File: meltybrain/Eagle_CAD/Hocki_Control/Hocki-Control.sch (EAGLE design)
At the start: 1 part, among them U1 TEENSY_4.1

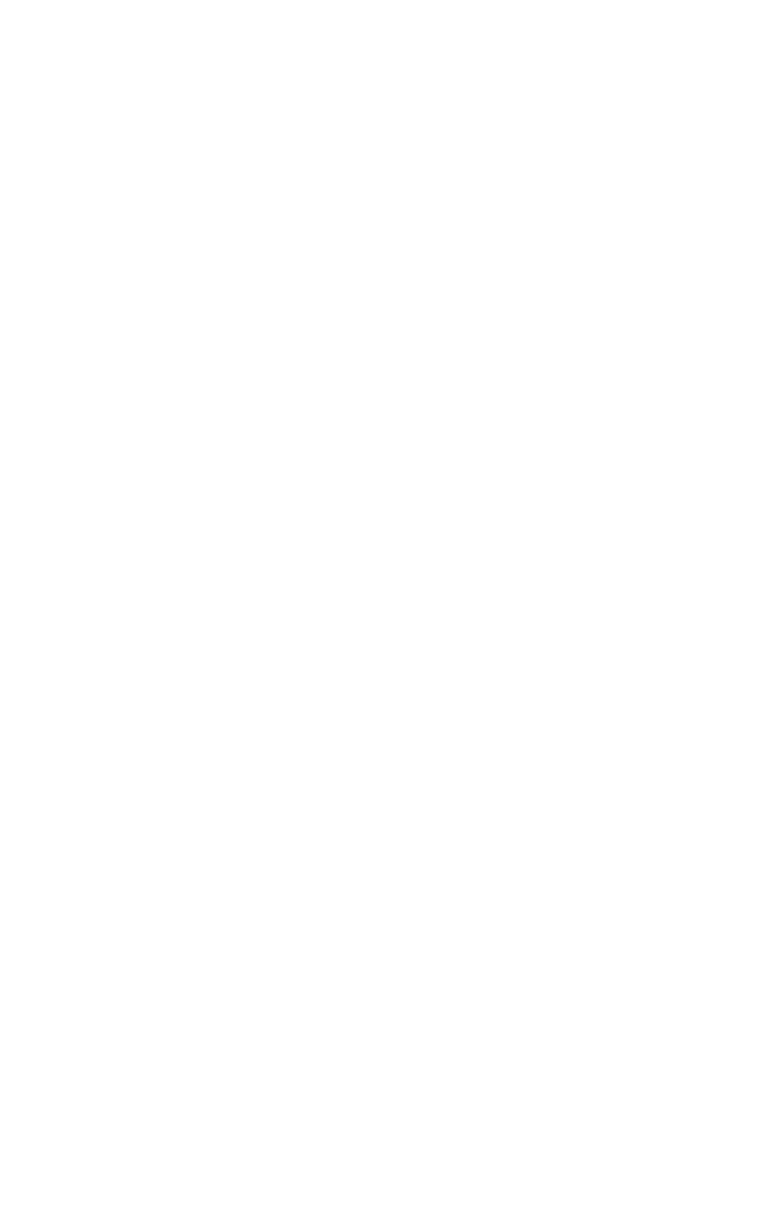
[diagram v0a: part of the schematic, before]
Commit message: added accelerometers to schematic
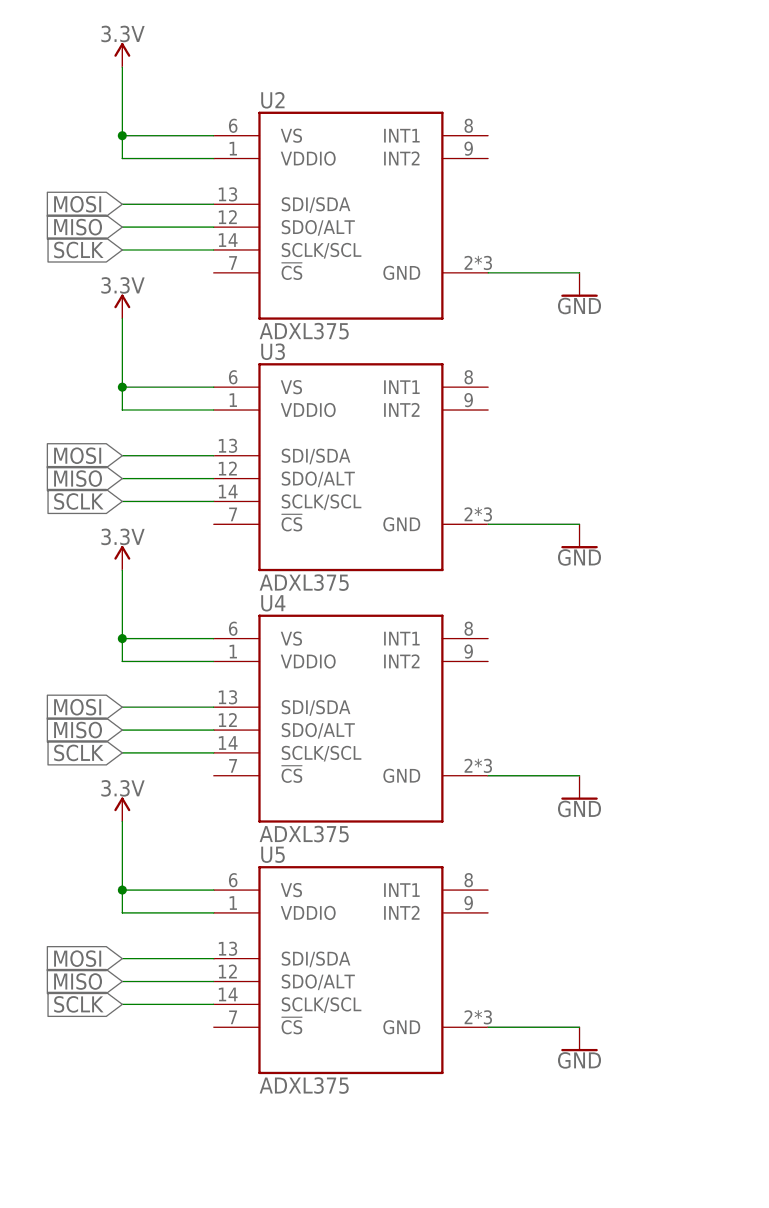
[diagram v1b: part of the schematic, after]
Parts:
- added U2, U3, U4, U5: ADXL375, Hocki_library:ADXL375
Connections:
- new net 3.3V: U2.VDDIO, U2.VS, U3.VDDIO, U3.VS, U4.VDDIO, U4.VS, U5.VDDIO, U5.VS
- new net GND: U2.GND, U3.GND, U4.GND, U5.GND
- new net MISO: U2.SDO/ALT, U3.SDO/ALT, U4.SDO/ALT, U5.SDO/ALT
- new net MOSI: U2.SDI/SDA, U3.SDI/SDA, U4.SDI/SDA, U5.SDI/SDA
- new net SCLK: U2.SCLK/SCL, U3.SCLK/SCL, U4.SCLK/SCL, U5.SCLK/SCL

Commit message: added bandpass filter to control and updated ir
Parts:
- added C1, C2: 100n, rcl:C-USC0603
- added C3, C4: 50n, rcl:C-USC0603
- added C5, C6: 60n, rcl:C-USC0603
- added D1, D2: RB521S30T1G, Hocki_library:RB521S30T1G
- added R1, R15, R18, R19: 50, rcl:R-US_R0603
- added R10, R11, R4, R5: 4.5k, rcl:R-US_R0603
- added R12, R13, R14, R3, R6, R7, R8, R9: 160, rcl:R-US_R0603
- added R16, R17: 45.25k, rcl:R-US_R0603
- added R2: 500, rcl:R-US_R0603
- added U10: TLV3502AIDCNR, Hocki_library:TLV3502AIDCNR
- added U6, U7, U8, U9: LMH6612MAX/NOPB, Hocki_library:LMH6612MAX/NOPB
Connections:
- new net 10K_INT: U10.OUTA, U10.OUTB
- new net 10K_PEAK: C6.1, D1.C, R17.2, U10.INA+, U9.INA-
- new net 10K_REF: U10.INA-
- new net 2.5V_REF: C2.2, C4.2, R10.1, R13.1, R4.1, R7.1, U6.INB-, U6.OUTB
- new net 20K_PEAK: C5.1, D2.C, R16.2, U10.INB+, U9.INB-
- new net 20K_REF: U10.INB-
- new net 5V: U6.V+, U7.V+, U8.V+, U9.V+
- new net N$1: R11.2, R5.2, U6.INA-, U6.OUTA
- new net N$10: C3.1, R12.1, U8.INA-, U8.INB-
- new net N$11: C4.1, R10.2, R11.1, R9.1, U8.INA+
- new net N$12: R12.2, R14.1, U8.OUTA, U9.INB+
- new net N$13: R13.2, R14.2, U8.INB+
- new net N$14: D1.A, R1.2, R18.1
- new net N$15: D2.A, R15.2, R19.1
- new net N$2: R1.1, U9.OUTA
- new net N$3: C1.2, R3.2, U7.OUTB
- new net N$4: C1.1, R6.1, U7.INA-, U7.INB-
- new net N$5: C2.1, R3.1, R4.2, R5.1, U7.INA+
- new net N$6: R6.2, R8.1, U7.OUTA, U9.INA+
- new net N$7: R7.2, R8.2, U7.INB+
- new net N$8: C3.2, R9.2, U8.OUTB
- new net N$9: R15.1, U9.OUTB
- new net VG_SIGNAL1: R2.2, U6.INA+
- net 3.3V: now also U10.V+
- net GND: now also C5.2, C6.2, R16.1, R17.1, R18.2, R19.2, R2.1, U10.V-, U6.V-, U7.V-, U8.V-, U9.V-
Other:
- moved on the sheet: U1, U2, U3, U4, U5

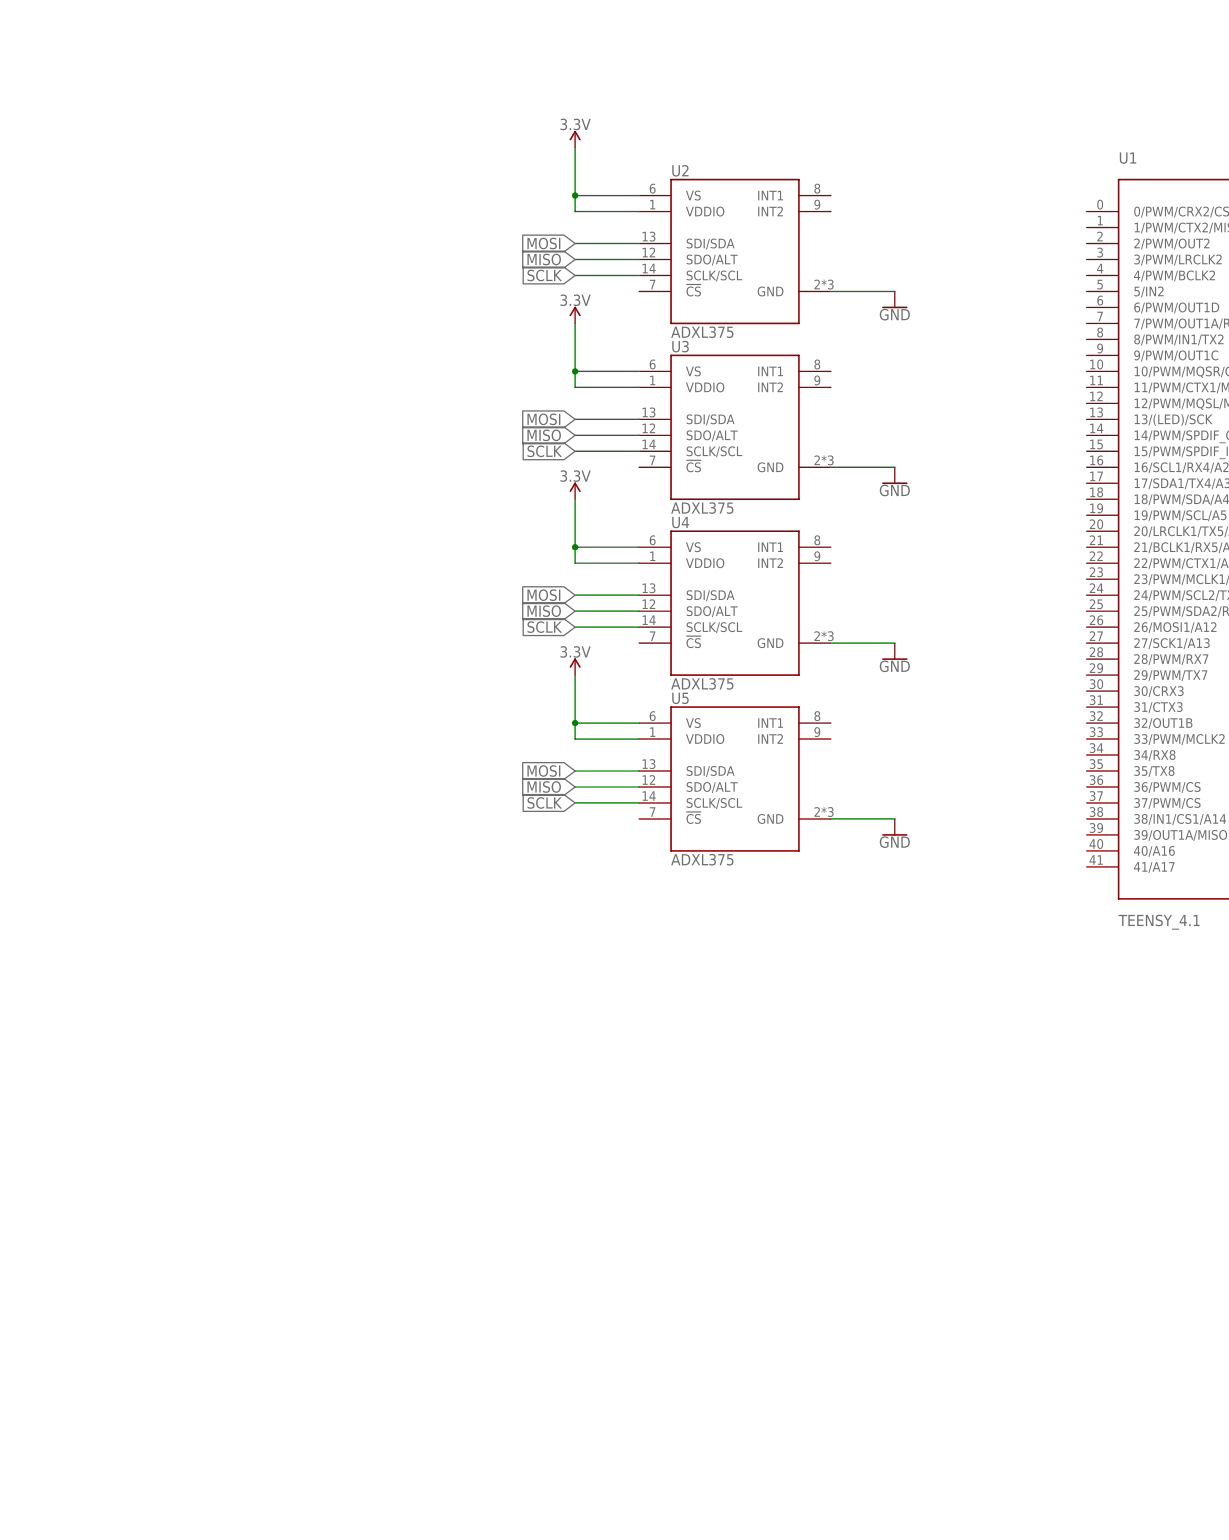
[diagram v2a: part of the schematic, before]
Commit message: magnetometer and accelerometer to schematic
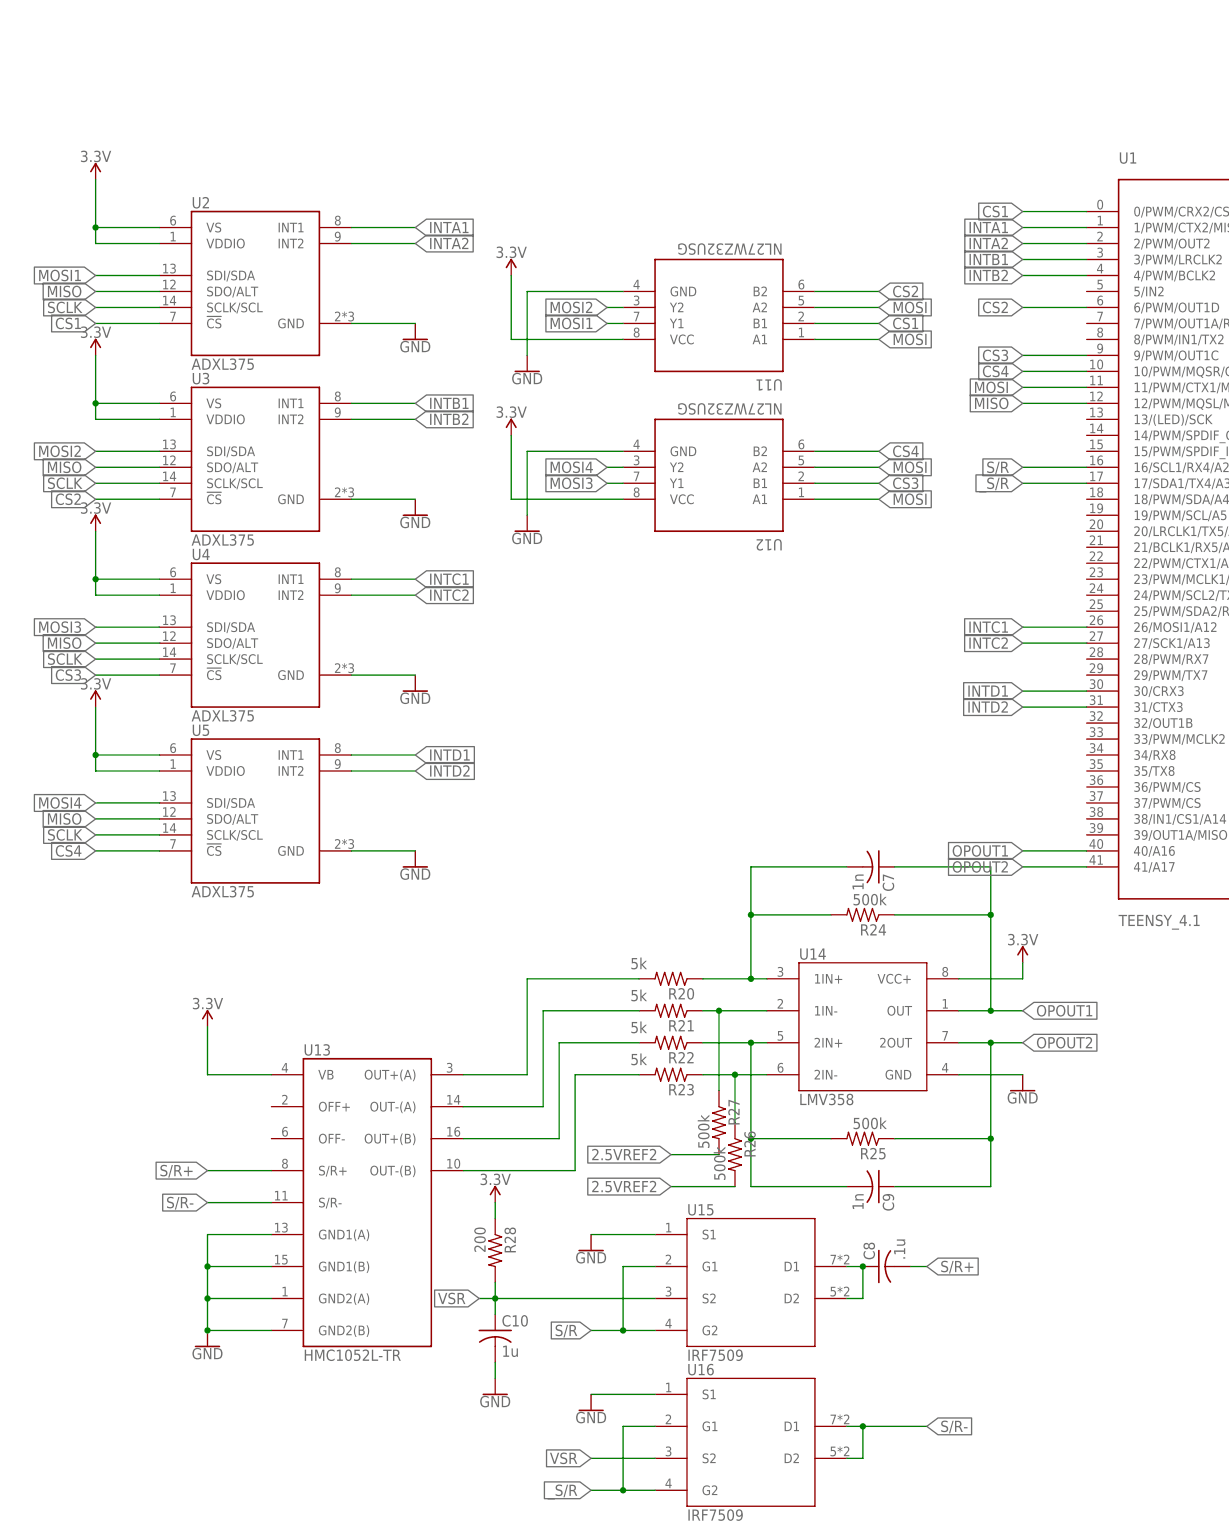
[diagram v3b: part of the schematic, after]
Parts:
- added C10: 1u, rcl:C-USC0603
- added C7, C9: 1n, rcl:C-USC0603
- added C8: .1u, rcl:C-USC0603
- added R20, R21, R22, R23: 5k, rcl:R-US_R0603
- added R24, R25, R26, R27: 500k, rcl:R-US_R0603
- added R28: 200, rcl:R-US_R0603
- added U11, U12: NL27WZ32USG, Hocki_library:NL27WZ32USG
- added U13: HMC1052L-TR, Hocki_library:HMC1052L-TR
- added U14: LMV358, Hocki_library:LMV358
- added U15, U16: IRF7509, Hocki_library:IRF7509
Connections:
- new net 2.5VREF2: R26.2, R27.2
- new net CS1: U1.0/PWM/CRX2/CS1/RX1, U11.B1, U2.!CS
- new net CS2: U1.6/PWM/OUT1D, U11.B2, U3.!CS
- new net CS3: U1.9/PWM/OUT1C, U12.B1, U4.!CS
- new net CS4: U1.10/PWM/MQSR/CS, U12.B2, U5.!CS
- new net INTA1: U1.1/PWM/CTX2/MISO1/TX1, U2.INT1
- new net INTA2: U1.2/PWM/OUT2, U2.INT2
- new net INTB1: U1.3/PWM/LRCLK2, U3.INT1
- new net INTB2: U1.4/PWM/BCLK2, U3.INT2
- new net INTC1: U1.26/MOSI1/A12, U4.INT1
- new net INTC2: U1.27/SCK1/A13, U4.INT2
- new net INTD1: U1.30/CRX3, U5.INT1
- new net INTD2: U1.31/CTX3, U5.INT2
- new net MOSI1: U11.Y1, U2.SDI/SDA
- new net MOSI2: U11.Y2, U3.SDI/SDA
- new net MOSI3: U12.Y1, U4.SDI/SDA
- new net MOSI4: U12.Y2, U5.SDI/SDA
- new net N$16: C8.1, U15.D1, U15.D2
- new net N$17: R21.2, U13.OUT-(A)
- new net N$18: R22.2, U13.OUT+(B)
- new net N$19: R23.2, U13.OUT-(B)
- new net N$34: R23.1, R26.1, U14.2IN-
- new net N$35: C9.2, R22.1, R25.2, U14.2IN+
- new net N$36: R21.1, R27.1, U14.1IN-
- new net N$37: C7.2, R20.1, R24.2, U14.1IN+
- new net OPOUT1: C7.1, R24.1, U1.40/A16, U14.OUT
- new net OPOUT2: C9.1, R25.1, U1.41/A17, U14.2OUT
- new net OUT+(A): R20.2, U13.OUT+(A)
- new net S/R: U1.16/SCL1/RX4/A2, U15.G1, U15.G2
- new net S/R+: C8.2, U13.S/R+
- new net S/R-: U13.S/R-, U16.D1, U16.D2
- new net VSR: C10.1, R28.2, U15.S2, U16.S2
- new net _S/R: U1.17/SDA1/TX4/A3, U16.G1, U16.G2
- net 3.3V: now also R28.1, U11.VCC, U12.VCC, U13.VB, U14.VCC+
- net GND: now also C10.2, U11.GND, U12.GND, U13.GND1(A), U13.GND1(B), U13.GND2(A), U13.GND2(B), U14.GND, U15.S1, U16.S1
- net MISO: now also U1.12/PWM/MQSL/MISO
- net MOSI: now also U1.11/PWM/CTX1/MOSI, U11.A1, U11.A2, U12.A1, U12.A2; no longer U2.SDI/SDA, U3.SDI/SDA, U4.SDI/SDA, U5.SDI/SDA
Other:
- moved on the sheet: U2, U3, U4, U5

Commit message: finished sensor circuits on control
IR mux
cleaned acc
magnetometer vref; did not need second set of mosfets
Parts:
- added C11, C12: 1u, rcl:C-USC0603
- added R29, R30, R33, R34, R35: 500, rcl:R-US_R0603
- added R31, R32: 5k, rcl:R-US_R0603
- added U17: LMH6612MAX/NOPB, Hocki_Library:LMH6612MAX/NOPB
- D1, D2: device Hocki_library:RB521S30T1G -> Hocki_Library:RB521S30T1G
- U1: device Hocki_library:TEENSY_4.1 -> Hocki_Library:TEENSY_4.1
- U10: device Hocki_library:TLV3502AIDCNR -> Hocki_Library:TLV3502AIDCNR
- U11, U12: device Hocki_library:NL27WZ32USG -> Hocki_Library:NL27WZ32USG
- U13: device Hocki_library:HMC1052L-TR -> Hocki_Library:HMC1052L-TR
- U14: device Hocki_library:LMV358 -> Hocki_Library:LMV358
- U15: device Hocki_library:IRF7509 -> Hocki_Library:IRF7509
- U16: value IRF7509 -> TMUX1219DCKR; device Hocki_library:IRF7509 -> Hocki_Library:TMUX1219DCKR
- U2, U3, U4, U5: device Hocki_library:ADXL375 -> Hocki_Library:ADXL375
- U6, U7, U8, U9: device Hocki_library:LMH6612MAX/NOPB -> Hocki_Library:LMH6612MAX/NOPB
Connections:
- net OPOUT1 renamed MAG_OUTPUTA
- net OPOUT2 renamed MAG_OUTPUTB
- removed net 2.5VREF2: R26.2, R27.2
- removed net S/R-: U13.S/R-, U16.D1, U16.D2
- new net 20K_INT: U1.23/PWM/MCLK1/CRX1/A9, U10.OUTB
- new net IR_BOTTOM: U16.S2
- new net IR_SEL: U1.17/SDA1/TX4/A3, U16.SEL
- new net IR_TOP: U16.S1
- new net N$20: R29.1, R30.2, U6.INB+
- new net N$21: R31.1, U1.18/PWM/SDA/A4
- new net N$22: R32.1, U1.19/PWM/SCL/A5
- new net N$23: R34.2, R35.1, U17.INA+, U17.INB+
- new net N$24: R33.1, U17.OUTB
- new net VREF/2: R26.2, R27.2, U17.INA-, U17.OUTA
- net 10K_INT: now also U1.22/PWM/CTX1/A8; no longer U10.OUTB
- net 10K_PEAK: now also U1.20/LRCLK1/TX5/A6
- net 10K_REF: now also C12.1, R31.2
- net 20K_PEAK: now also U1.21/BCLK1/RX5/A7
- net 20K_REF: now also C11.1, R32.2
- net 3.3V: now also R34.1, U17.V+
- net 5V: now also R29.2, U1.VIN, U16.V+
- net GND: now also C11.2, C12.2, R30.1, R33.2, R35.2, U1.GND, U13.OFF-, U13.S/R-, U16.GND, U17.INB-, U17.V-; no longer U16.S1
- net VG_SIGNAL1: now also U16.D
- net VSR: no longer U16.S2
- net _S/R: now also U1.15/PWM/SPDIF_IN/RX3/A1; no longer U1.17/SDA1/TX4/A3, U16.G1, U16.G2
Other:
- moved on the sheet: C1, C10, C2, C3, C4, C5, C6, C7, C8, C9, D1, D2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

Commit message: progress...
IR receiver has all parts accounting BoM
started doing that for control
progress on control layout
Varun I hate this...
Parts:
- removed R1, R15, R18, R19: 50, rcl:R-US_R0603
- added C13, C15: 0.5u, rcl:C-USC0603
- added C14, C16: 2u, rcl:C-USC0603
- added R36, R38: 5k, rcl:R-US_R0603
- added R37, R39: 820, rcl:R-US_R0603
- added U18: LMV358, Hocki_Library:LMV358
- C1, C2: value 100n -> 47n; device rcl:C-USC0603 -> rcl:C-USC1206
- C3, C4: value 50n -> 47n; device rcl:C-USC0603 -> rcl:C-USC1206
- R12, R13, R14, R9: value 160 -> 169
- R16, R17: value 45.25k -> 44.2k
- R2, R33, R34, R35: value 500 -> 499
- R29: value 500 -> 665
- R30: value 500 -> 330
- U17: value LMH6612MAX/NOPB -> LMV358; device Hocki_Library:LMH6612MAX/NOPB -> Hocki_Library:LMV358
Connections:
- net N$1 renamed VG_SIGNAL_BUF
- net N$12 renamed 20K_OUT
- net N$20 renamed 1.6V_REF
- net N$6 renamed 10K_OUT
- net VG_SIGNAL1 renamed VG_SIGNAL
- removed net 2.5V_REF: C2.2, C4.2, R10.1, R13.1, R4.1, R7.1, U6.INB-, U6.OUTB
- removed net N$11: C4.1, R10.2, R11.1, R9.1, U8.INA+
- removed net N$14: D1.A, R1.2, R18.1
- removed net N$15: D2.A, R15.2, R19.1
- removed net N$3: C1.2, R3.2, U7.OUTB
- removed net N$5: C2.1, R3.1, R4.2, R5.1, U7.INA+
- removed net N$8: C3.2, R9.2, U8.OUTB
- new net 1.66V_REF_BUF: C1.2, C3.2, R10.1, R13.1, R4.1, R7.1, U6.INB-, U6.OUTB
- new net 10K_FB: C2.2, R3.2, U7.OUTB
- new net 10K_IN: C1.1, R3.1, R4.2, R5.1, U7.INA+
- new net 20K_FB: C4.2, R9.2, U8.OUTB
- new net 20K_IN: C3.1, R10.2, R11.1, R9.1, U8.INA+
- new net MAG_FILT_A: C14.2, U1.40/A16, U18.1IN-, U18.OUT
- new net MAG_FILT_B: C16.2, U1.41/A17, U18.2IN-, U18.2OUT
- new net MAG_OUTPUTA1: R38.2
- new net N$25: C14.1, R36.1, R37.2
- new net N$26: C13.1, R37.1, U18.1IN+
- new net N$29: C16.1, R38.1, R39.2
- new net N$30: C15.1, R39.1, U18.2IN+
- net 3.3V: now also U17.VCC+, U9.V+; no longer U14.VCC+, U17.V+
- net 5V: now also U14.VCC+, U18.VCC+; no longer U9.V+
- net GND: now also C13.2, C15.2, U17.2IN+, U17.2IN-, U17.GND, U18.GND; no longer R18.2, R19.2, U17.INB-, U17.V-
- net MAG_OUTPUTA: now also R36.2; no longer U1.40/A16
- net MAG_OUTPUTB: no longer U1.41/A17
- net N$10: now also C4.1; no longer C3.1
- net N$2: now also D1.A; no longer R1.1
- net N$23: now also U17.1IN+; no longer U17.INA+, U17.INB+
- net N$24: now also U17.2OUT; no longer U17.OUTB
- net N$4: now also C2.1; no longer C1.1
- net N$9: now also D2.A; no longer R15.1
- net VREF/2: now also U17.1IN-, U17.OUT; no longer U17.INA-, U17.OUTA
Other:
- moved on the sheet: C1, C2, C3, C4, C5, C6, D1, D2, R16, R17, R34, R35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

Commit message: good progress on control
edited mag footprint once again...pads were flagged by drc
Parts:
- added C17, C18, C19, C20, C21, C22, C23, C24, C25, C26, C27, C28, C29, C30, C31, C32, C33, C34, C35, C36, C37: 0.1u, rcl:C-USC0603
- C5, C6: value 60n -> 62n; device rcl:C-USC0603 -> Hocki_Library:BFC241646203
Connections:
- net N$17 renamed OUT-(A)
- net N$18 renamed OUT+(B)
- net N$19 renamed OUT-(B)
- removed net INTA1: U1.1/PWM/CTX2/MISO1/TX1, U2.INT1
- removed net INTA2: U1.2/PWM/OUT2, U2.INT2
- removed net INTB1: U1.3/PWM/LRCLK2, U3.INT1
- removed net INTB2: U1.4/PWM/BCLK2, U3.INT2
- removed net INTC1: U1.26/MOSI1/A12, U4.INT1
- removed net INTC2: U1.27/SCK1/A13, U4.INT2
- removed net INTD1: U1.30/CRX3, U5.INT1
- removed net INTD2: U1.31/CTX3, U5.INT2
- removed net _S/R: U1.15/PWM/SPDIF_IN/RX3/A1
- new net INT1A: U1.40/A16, U2.INT1
- new net INT1B: U1.41/A17, U2.INT2
- new net INT2A: U1.16/SCL1/RX4/A2, U3.INT1
- new net INT2B: U1.17/SDA1/TX4/A3, U3.INT2
- new net INT3A: U1.8/PWM/IN1/TX2, U4.INT1
- new net INT3B: U1.7/PWM/OUT1A/RX2, U4.INT2
- new net INT4A: U1.25/PWM/SDA2/RX6/A11, U5.INT1
- new net INT4B: U1.24/PWM/SCL2/TX6/A10, U5.INT2
- net 10K_PEAK: now also C5.1; no longer C6.1
- net 20K_PEAK: now also C6.1; no longer C5.1
- net 3.3V: now also C22.1, C23.1, C24.1, C25.1, C26.1, C27.1, C28.1, C29.1, C30.1, C31.1, C32.1, C33.1, C34.1, C35.1, C36.1, C37.1, U14.VCC+, U18.VCC+
- net 5V: now also C17.1, C18.1, C19.1, C20.1, C21.1; no longer U14.VCC+, U18.VCC+
- net CS1: now also U1.14/PWM/SPDIF_OUT/TX3/A0; no longer U1.0/PWM/CRX2/CS1/RX1
- net CS2: now also U1.15/PWM/SPDIF_IN/RX3/A1; no longer U1.6/PWM/OUT1D
- net GND: now also C17.2, C18.2, C19.2, C20.2, C21.2, C22.2, C23.2, C24.2, C25.2, C26.2, C27.2, C28.2, C29.2, C30.2, C31.2, C32.2, C33.2, C34.2, C35.2, C36.2, C37.2
- net IR_SEL: now also U1.36/PWM/CS; no longer U1.17/SDA1/TX4/A3
- net MAG_FILT_A: now also U1.38/IN1/CS1/A14; no longer U1.40/A16
- net MAG_FILT_B: now also U1.39/OUT1A/MISO1/A15; no longer U1.41/A17
- net S/R: now also U1.33/PWM/MCLK2; no longer U1.16/SCL1/RX4/A2
- net SCLK: now also U1.13/(LED)/SCK
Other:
- moved on the sheet: C14, C5, C6, C7, R24, R33, R34, R35, U11, U12, U17
